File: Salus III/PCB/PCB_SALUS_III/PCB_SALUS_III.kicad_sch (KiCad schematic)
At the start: 52 parts, among them J1 Conn_01x20_Pin, J2 Conn_01x20_Pin, K1 Relay_SPDT, U1 ESP32-DEVKITC-32D

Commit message: Se completo la investigacion y se agregaron simulaciones de Circuitos de proteccion
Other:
- note added: "En el diagrama de circuito esta dada vuelta la tira de pinas, eso hay que cambiarlo Y agregar un Pin mas de 5V para que le de la corriente a la Rasp"
- note added: "Voy a modificar el valor de la resistencia del zener por una de 1K para que encienda correctamente"
- note removed: "En el diagrama de circuito esta dada vuelta la tira de pinas, eso hay que cambiarlo"
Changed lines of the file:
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@@
 	(text "RASP"
 		(exclude_from_sim no)
-		(at 65.278 96.52 0)
+		(at 53.34 107.188 0)
 		(effects
 			(font
@@
 		)
 	)
-	(text "En el diagrama de circuito esta dada vuelta la tira de pinas, eso hay que cambiarlo\n"
+	(text "En el diagrama de circuito esta dada vuelta la tira de pinas, eso hay que cambiarlo \nY agregar un Pin mas de 5V para que le de la corriente a la Rasp\n\n"
 		(exclude_from_sim no)
-		(at -34.544 135.382 0)
+		(at -21.336 131.064 0)
 		(effects
 			(font
@@
 		)
 	)
+	(text "Voy a modificar el valor de la resistencia del zener por una de 1K para que encienda correctamente"
+		(exclude_from_sim no)
+		(at 267.208 53.086 0)
+		(effects
+			(font
+				(size 1.27 1.27)
+			)
+		)
+	)
 	(text "Gpio 16"
 		(exclude_from_sim no)
@@
 	(text "ESP32\n"
 		(exclude_from_sim no)
-		(at 64.008 29.21 0)
+		(at 65.024 33.02 0)
 		(effects
 			(font

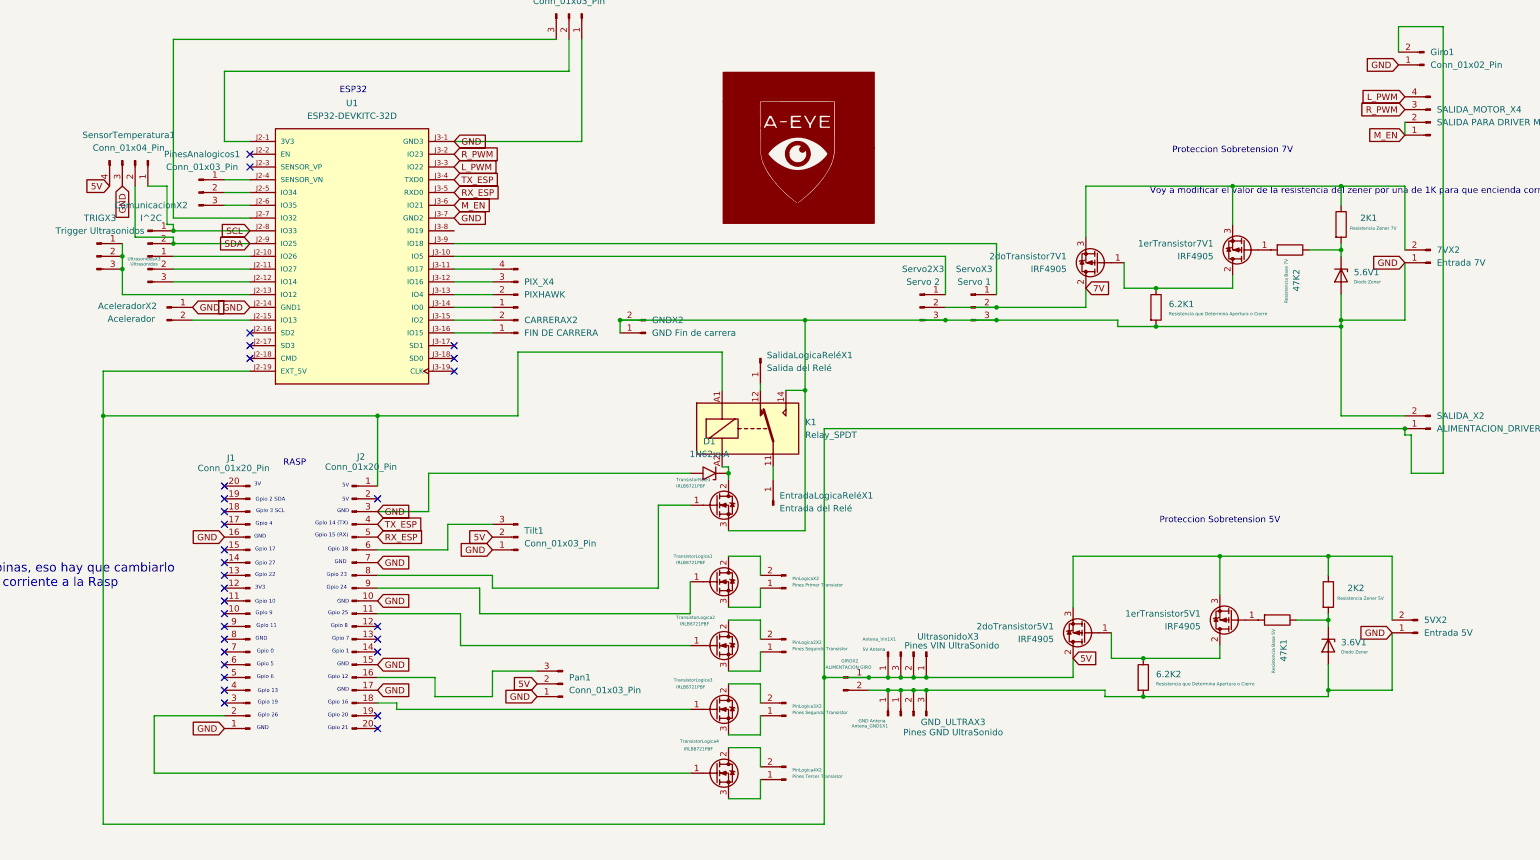
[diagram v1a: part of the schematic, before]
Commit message: se agrego logica de Rasp y algunos conectores
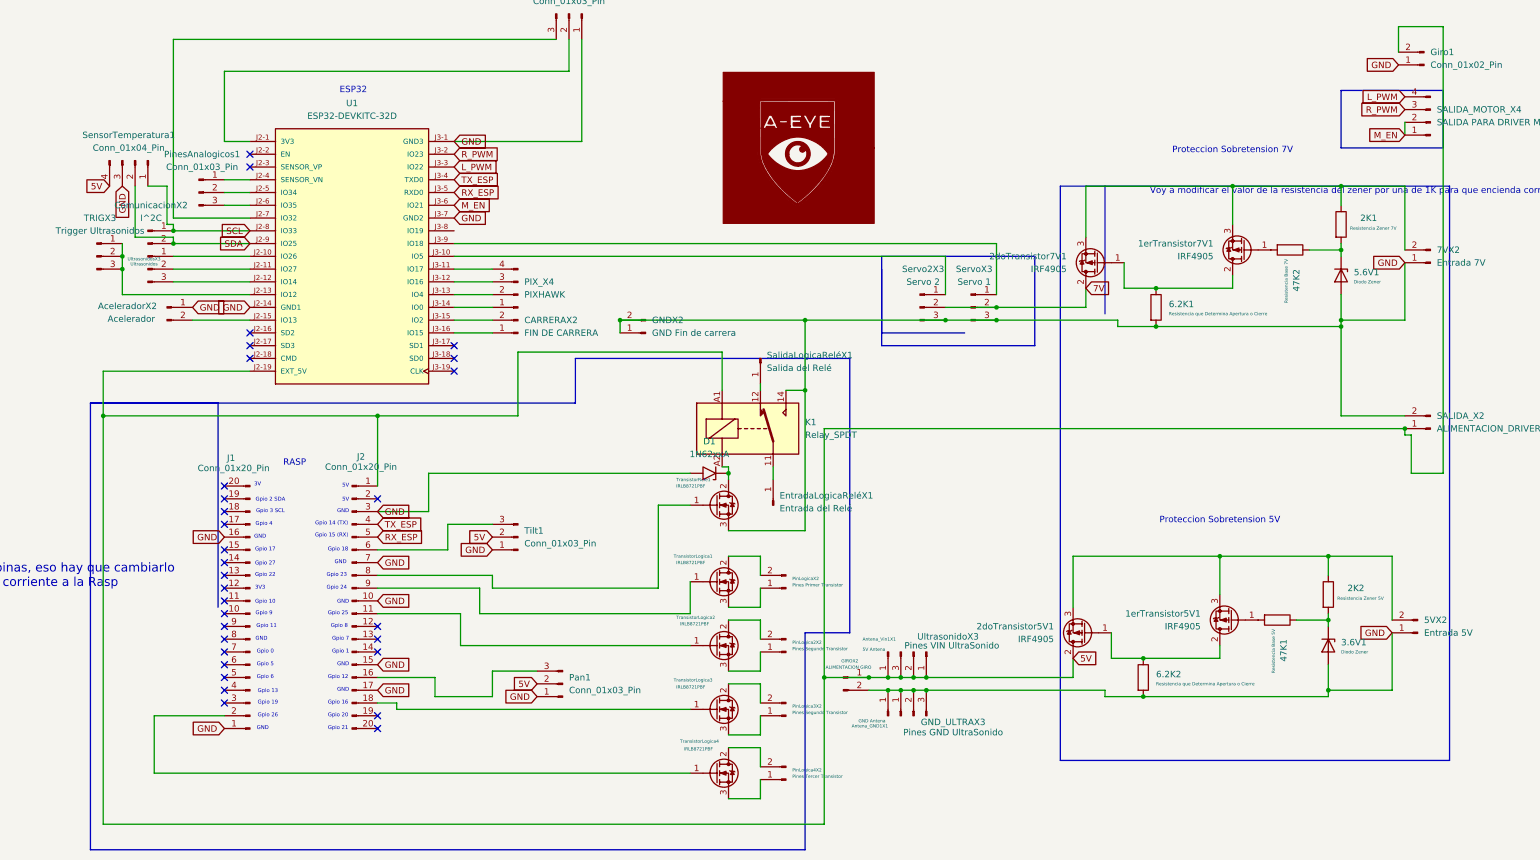
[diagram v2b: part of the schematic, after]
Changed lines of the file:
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@@
+		)
+	)
+	(polyline
+		(pts
+			(xy 12.7 95.25) (xy 109.22 95.25)
+		)
+		(stroke
+			(width 0)
+			(type default)
 		)
 	)
@@
 		)
 	)
+	(polyline
+		(pts
+			(xy 163.83 140.97) (xy 154.94 140.97)
+		)
+		(stroke
+			(width 0)
+			(type default)
+		)
+	)
 	(wire
 		(pts
@@
 		)
 	)
+	(polyline
+		(pts
+			(xy 261.62 33.02) (xy 261.62 44.45)
+		)
+		(stroke
+			(width 0)
+			(type default)
+		)
+	)
 	(wire
 		(pts
@@
 		)
 	)
+	(polyline
+		(pts
+			(xy 261.62 44.45) (xy 281.94 44.45)
+		)
+		(stroke
+			(width 0)
+			(type default)
+		)
+	)
 	(wire
 		(pts
@@
 		)
 	)
+	(polyline
+		(pts
+			(xy 200.66 83.82) (xy 200.66 66.04)
+		)
+		(stroke
+			(width 0)
+			(type default)
+		)
+	)
 	(wire
 		(pts
@@
 		)
 	)
+	(polyline
+		(pts
+			(xy 170.18 68.58) (xy 170.18 83.82)
+		)
+		(stroke
+			(width 0)
+			(type default)
+		)
+	)
 	(wire
 		(pts
@@
 		)
 	)
+	(polyline
+		(pts
+			(xy 261.62 33.02) (xy 281.94 33.02)
+		)
+		(stroke
+			(width 0)
+			(type default)
+		)
+	)
 	(wire
 		(pts
@@
 		)
 	)
+	(polyline
+		(pts
+			(xy 38.1 95.25) (xy 38.1 135.89)
+		)
+		(stroke
+			(width 0)
+			(type default)
+		)
+	)
 	(wire
 		(pts
@@
 		)
 	)
+	(polyline
+		(pts
+			(xy 12.7 95.25) (xy 38.1 95.25)
+		)
+		(stroke
+			(width 0)
+			(type default)
+		)
+	)
 	(wire
 		(pts
@@
 		)
 	)
+	(polyline
+		(pts
+			(xy 283.21 166.37) (xy 283.21 52.07)
+		)
+		(stroke
+			(width 0)
+			(type default)
+		)
+	)
 	(wire
 		(pts
@@
 		)
 	)
+	(polyline
+		(pts
+			(xy 205.74 166.37) (xy 283.21 166.37)
+		)
+		(stroke
+			(width 0)
+			(type default)
+		)
+	)
 	(wire
 		(pts
@@
 		)
 	)
+	(polyline
+		(pts
+			(xy 214.63 52.07) (xy 214.63 77.47)
+		)
+		(stroke
+			(width 0)
+			(type default)
+		)
+	)
 	(wire
 		(pts
@@
 		)
 	)
+	(polyline
+		(pts
+			(xy 170.18 66.04) (xy 170.18 81.28)
+		)
+		(stroke
+			(width 0)
+			(type default)
+		)
+	)
 	(wire
 		(pts
@@
 		)
 	)
+	(polyline
+		(pts
+			(xy 12.7 184.15) (xy 154.94 184.15)
+		)
+		(stroke
+			(width 0)
+			(type default)
+		)
+	)
 	(wire
 		(pts
@@
 		)
 	)
+	(polyline
+		(pts
+			(xy 281.94 44.45) (xy 281.94 33.02)
+		)
+		(stroke
+			(width 0)
+			(type default)
+		)
+	)
 	(wire
 		(pts
@@
 		)
 	)
+	(polyline
+		(pts
+			(xy 109.22 95.25) (xy 109.22 86.36)
+		)
+		(stroke
+			(width 0)
+			(type default)
+		)
+	)
 	(wire
 		(pts
@@
 		)
 	)
+	(polyline
+		(pts
+			(xy 170.18 83.82) (xy 200.66 83.82)
+		)
+		(stroke
+			(width 0)
+			(type default)
+		)
+	)
 	(wire
 		(pts
@@
 		)
 	)
+	(polyline
+		(pts
+			(xy 200.66 66.04) (xy 170.18 66.04)
+		)
+		(stroke
+			(width 0)
+			(type default)
+		)
+	)
 	(wire
 		(pts
@@
 		)
 	)
+	(polyline
+		(pts
+			(xy 205.74 52.07) (xy 283.21 52.07)
+		)
+		(stroke
+			(width 0)
+			(type default)
+		)
+	)
+	(polyline
+		(pts
+			(xy 12.7 184.15) (xy 12.7 95.25)
+		)
+		(stroke
+			(width 0)
+			(type default)
+		)
+	)
 	(wire
 		(pts
@@
 		)
 	)
+	(polyline
+		(pts
+			(xy 109.22 86.36) (xy 163.83 86.36)
+		)
+		(stroke
+			(width 0)
+			(type default)
+		)
+	)
+	(polyline
+		(pts
+			(xy 170.18 81.28) (xy 186.69 81.28)
+		)
+		(stroke
+			(width 0)
+			(type default)
+		)
+	)
 	(wire
 		(pts
@@
 		)
 	)
+	(polyline
+		(pts
+			(xy 205.74 52.07) (xy 205.74 166.37)
+		)
+		(stroke
+			(width 0)
+			(type default)
+		)
+	)
 	(wire
 		(pts
@@
 		)
 	)
+	(polyline
+		(pts
+			(xy 163.83 86.36) (xy 163.83 140.97)
+		)
+		(stroke
+			(width 0)
+			(type default)
+		)
+	)
 	(wire
 		(pts
@@
 		)
 		(stroke
+			(width 0)
+			(type default)
+		)
+	)
+	(polyline
+		(pts
+			(xy 154.94 140.97) (xy 154.94 184.15)
+		)
+		(stroke
